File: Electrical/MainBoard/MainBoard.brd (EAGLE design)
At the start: 100 x 100 mm, 126 parts, among them IC1 MEGA1284-P, IC2 MCP4922-E/SL, IC3 MCP4921-E/SN, IC4 TL074D, IC5 TL074D, IC6 FT232RL, Q1 BC140-10, Q2 BC160, Q3 BC140-10, Q4 BC160, Q5 BD239, Q6 BD240, Q7 BC557, Q8 16MHz, X1 FH12-45S-0.5SH, X2 22-23-2021, X3 PN61729-S

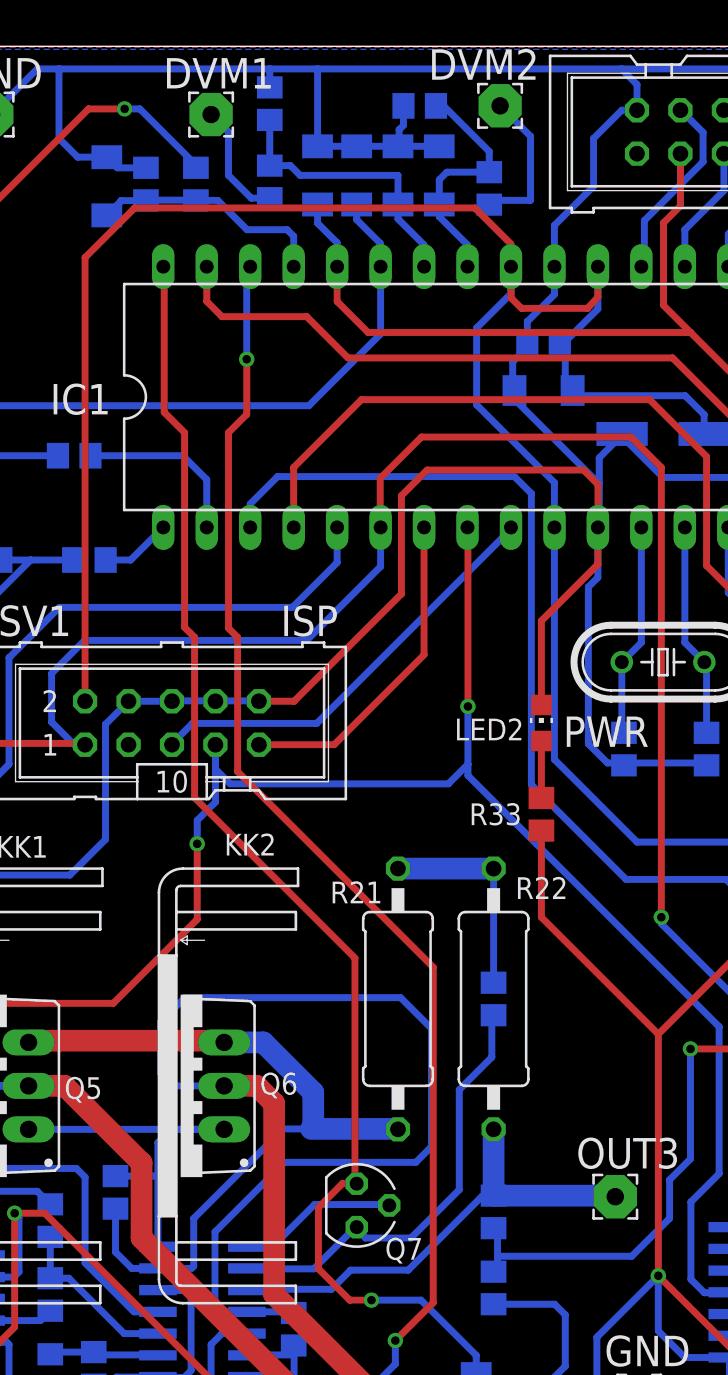
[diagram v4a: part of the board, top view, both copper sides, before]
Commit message: Removed some Z-Diodes, removed Resistor R20 (PowerSupply, between OpAmp IC5B and transistors Q5 and Q6)
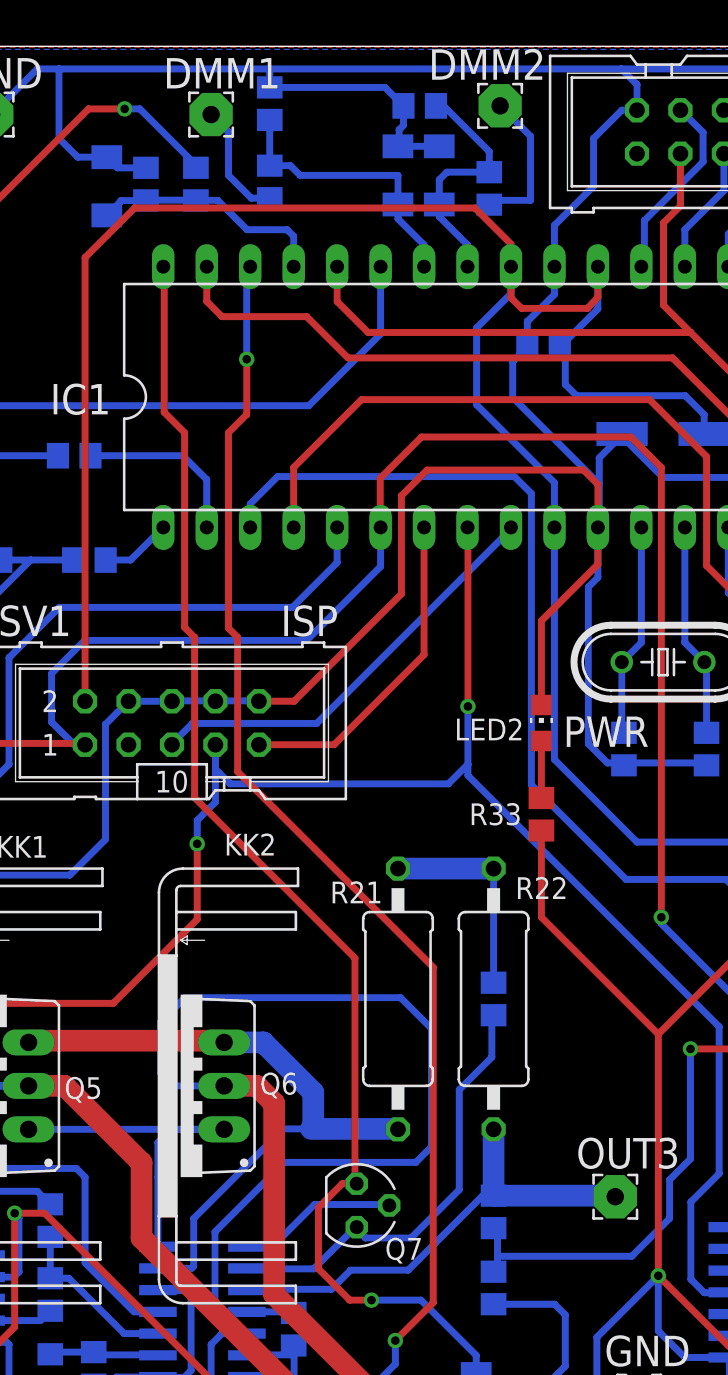
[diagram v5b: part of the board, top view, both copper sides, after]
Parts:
- removed D5, D6, D7: 5V, diode:SOD80C
- removed R20: 100R, OwnDevices:R0805
- renumbered DVM1 to DMM1, DVM2 to DMM2, GND_DVM to GND_DMM
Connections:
- net +3V3: no longer D6.C
- net +5V: no longer D5.C, D7.C
- net GND: no longer D5.A, D6.A, D7.A
- net N$18: no longer R20.2
- net N$20: no longer R20.1
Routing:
- net N$18: track 44.6 -> 39.2 mm
- net +3V3: track 213.9 -> 209.7 mm
- net +5V: track 634.1 -> 630.0 mm
- net N$20: track 24.2 -> 21.7 mm
- net GND: track 687.1 -> 685.4 mm

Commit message: Changed Resistor values of PowerSupply current measurement circuit (R21, R22, R23)
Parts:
- R21: value 4R7 -> 5R1
- R22: value 1R -> 0R1
- R23: value 1k -> 100R
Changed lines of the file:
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@@
 <drawing>
 <settings>
-<setting alwaysvectorfont="no"/>
+<setting alwaysvectorfont="yes"/>
 <setting verticaltext="up"/>
 </settings>
@@
 <attribute name="VALUE" x="52.578" y="35.306" size="1.778" layer="27" ratio="10" rot="R90"/>
 </element>
-<element name="R21" library="OwnDevices" library_urn="urn:adsk.eagle:library:19498084" package="0411/15" package3d_urn="urn:adsk.eagle:package:23568/2" value="4R7" x="67.818" y="44.323" smashed="yes" rot="R90">
+<element name="R21" library="OwnDevices" library_urn="urn:adsk.eagle:library:19498084" package="0411/15" package3d_urn="urn:adsk.eagle:package:23568/2" value="5R1" x="67.818" y="44.323" smashed="yes" rot="R90">
 <attribute name="NAME" x="66.929" y="51.181" size="1.27" layer="25" font="vector" ratio="15" rot="R180"/>
 <attribute name="POPULARITY" value="1" x="67.818" y="44.323" size="1.778" layer="27" rot="R90" display="off"/>
@@
 <attribute name="VALUE" x="68.453" y="42.0624" size="1.27" layer="27" ratio="10" rot="R90"/>
 </element>
-<element name="R22" library="OwnDevices" library_urn="urn:adsk.eagle:library:19498084" package="0411/15" package3d_urn="urn:adsk.eagle:package:23568/2" value="1R" x="73.406" y="44.323" smashed="yes" rot="R270">
+<element name="R22" library="OwnDevices" library_urn="urn:adsk.eagle:library:19498084" package="0411/15" package3d_urn="urn:adsk.eagle:package:23568/2" value="0R1" x="73.406" y="44.323" smashed="yes" rot="R270">
 <attribute name="NAME" x="74.676" y="50.165" size="1.27" layer="25" font="vector" ratio="15"/>
 <attribute name="POPULARITY" value="1" x="73.406" y="44.323" size="1.778" layer="27" rot="R270" display="off"/>
@@
 <attribute name="VALUE" x="72.771" y="46.5836" size="1.27" layer="27" ratio="10" rot="R270"/>
 </element>
-<element name="R23" library="OwnDevices" library_urn="urn:adsk.eagle:library:19498084" package="R0805" package3d_urn="urn:adsk.eagle:package:23553/2" value="1k" x="73.406" y="44.323" smashed="yes" rot="MR90">
+<element name="R23" library="OwnDevices" library_urn="urn:adsk.eagle:library:19498084" package="R0805" package3d_urn="urn:adsk.eagle:package:23553/2" value="100R" x="73.406" y="44.323" smashed="yes" rot="MR90">
 <attribute name="NAME" x="75.057" y="46.736" size="1.27" layer="26" font="vector" ratio="15" rot="MR0"/>
 <attribute name="POPULARITY" value="86" x="73.406" y="44.323" size="1.778" layer="28" rot="MR90" display="off"/>

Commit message: Changed power stage of PowerSupply channel
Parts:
- Q6: value BD240 -> BC547; device OwnDevices:CB-274 -> transistor:TO92
- moved KK2 13.8 mm to (41.0, 39.2), turned to 90 degrees
- moved Q6 1.28 mm to (55.0, 38.0), turned to 270 degrees
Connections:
- new net N$38: IC5.7, Q6.2
- net +12V: now also Q6.3
- net -12V: no longer Q6.T2
- net N$18: no longer Q6.G
- net N$20: now also Q6.1; no longer IC5.7, Q6.T1
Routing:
- net -12V: track 175.6 -> 108.9 mm, vias 0 -> 1
- net N$20: track 21.7 -> 8.76 mm
- net N$38: track 0.00 -> 9.42 mm
- net +12V: track 210.4 -> 219.2 mm
- net PS_CUR: track 80.4 -> 85.1 mm
- net N$18: track 39.2 -> 42.9 mm
- net -12V_VOLT: track 83.0 -> 84.2 mm
- net N$7: vias 0 -> 2

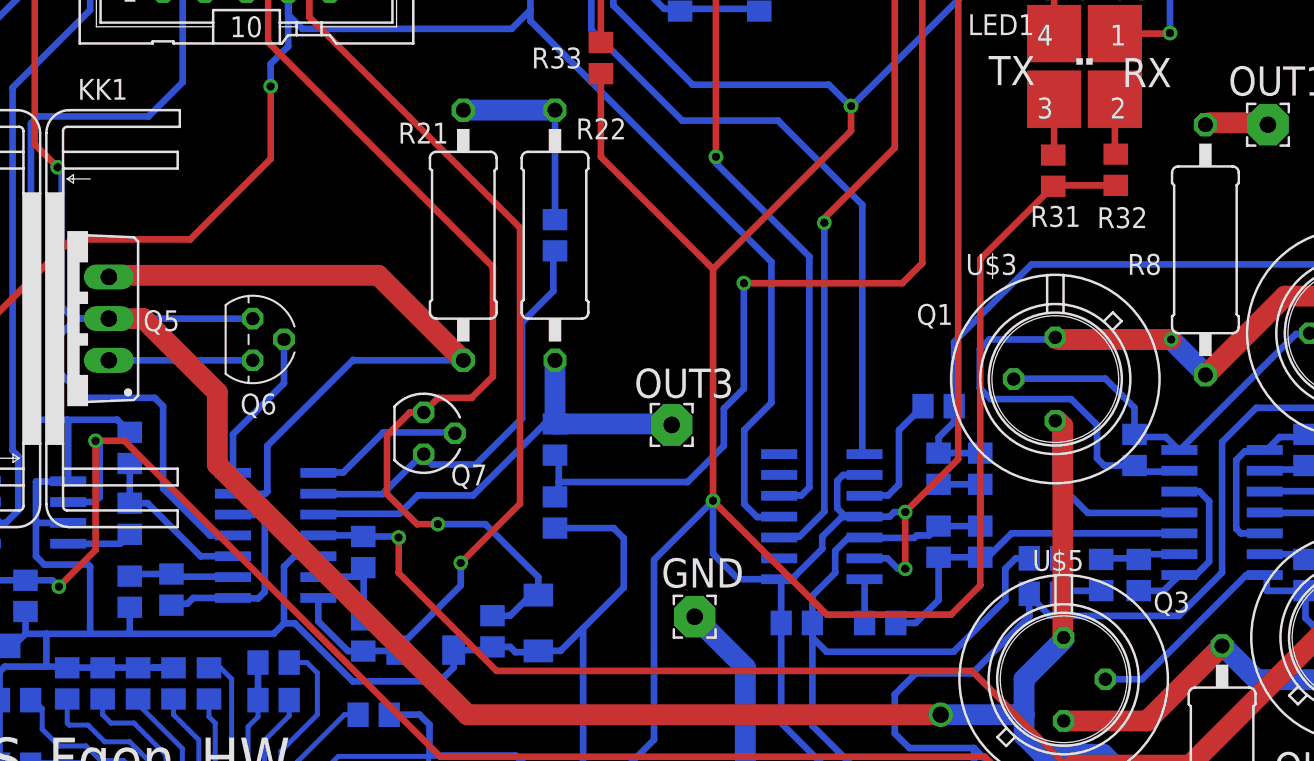
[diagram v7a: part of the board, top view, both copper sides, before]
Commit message: Removed Z-Diode D1 (PS_CUR), moved resistor R21 of current measurement circuit to be after this circuit
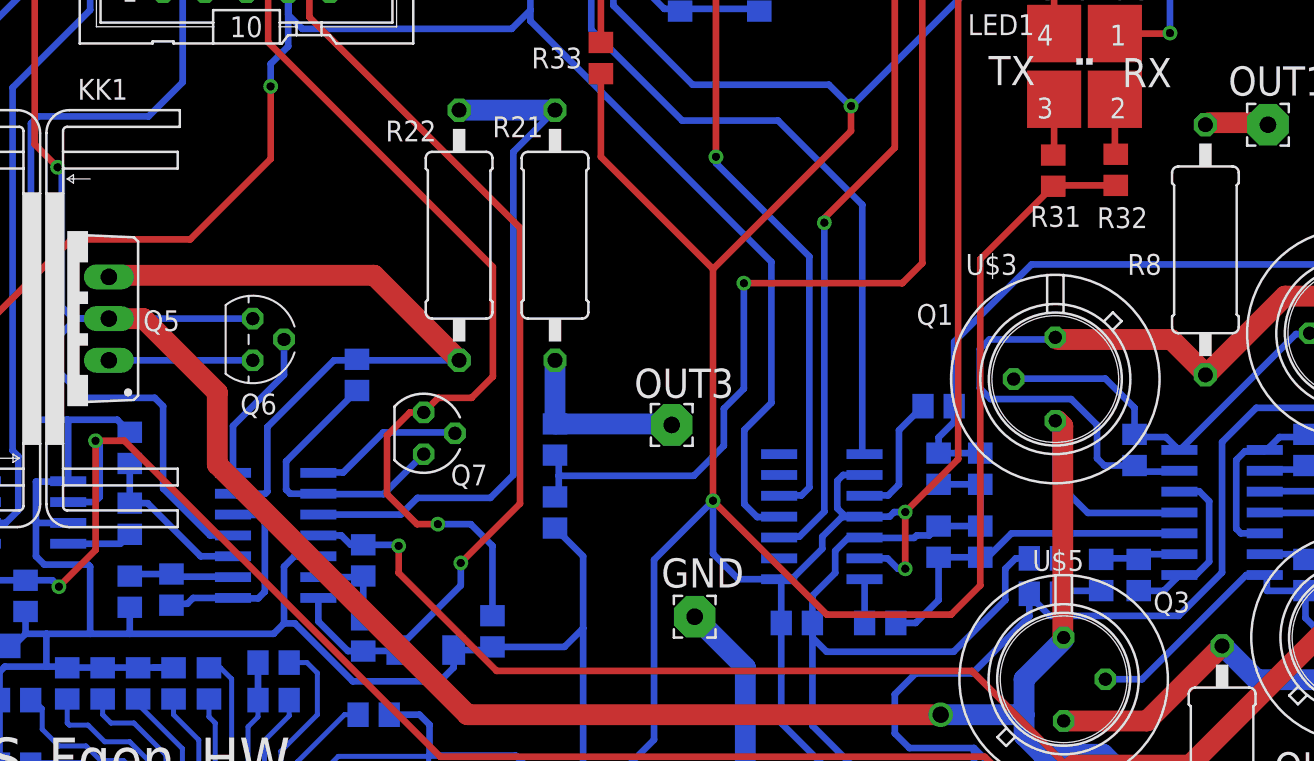
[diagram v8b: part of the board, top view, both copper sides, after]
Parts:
- removed D1: 5V, diode:SOD80C
- moved R23 14.8 mm to (61.3, 35.8)
- moved R22 5.84 mm to (67.6, 44.3), turned to 90 degrees
- moved R21 5.59 mm to (73.4, 44.3), turned to 270 degrees
- moved R27 0.51 mm to (61.7, 24.5)
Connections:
- removed net N$21: R21.2, R22.1, R23.2
- new net N$39: IC5.10, R21.1, R22.2
- net GND: no longer D1.A
- net N$18: now also R22.1, R23.2; no longer R21.1
- net N$22: now also R21.2; no longer IC5.10, R22.2
- net PS_CUR: no longer D1.C
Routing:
- net N$39: track 0.00 -> 42.0 mm
- net N$22: track 27.7 -> 11.0 mm
- net N$21: track 12.3 -> 0.00 mm
- net N$23: track 26.0 -> 17.3 mm
- net GND: track 685.4 -> 681.0 mm
- net PS_CUR: track 85.1 -> 81.3 mm
- net N$27: track 6.49 -> 5.39 mm
- net N$7: vias 2 -> 0
